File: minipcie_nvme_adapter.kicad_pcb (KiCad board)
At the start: 4 copper layers, 63.7 x 23.6 mm, 13 parts, among them J1 Bus_PCI_Express_Mini, J2 Bus_M.2_Socket_M

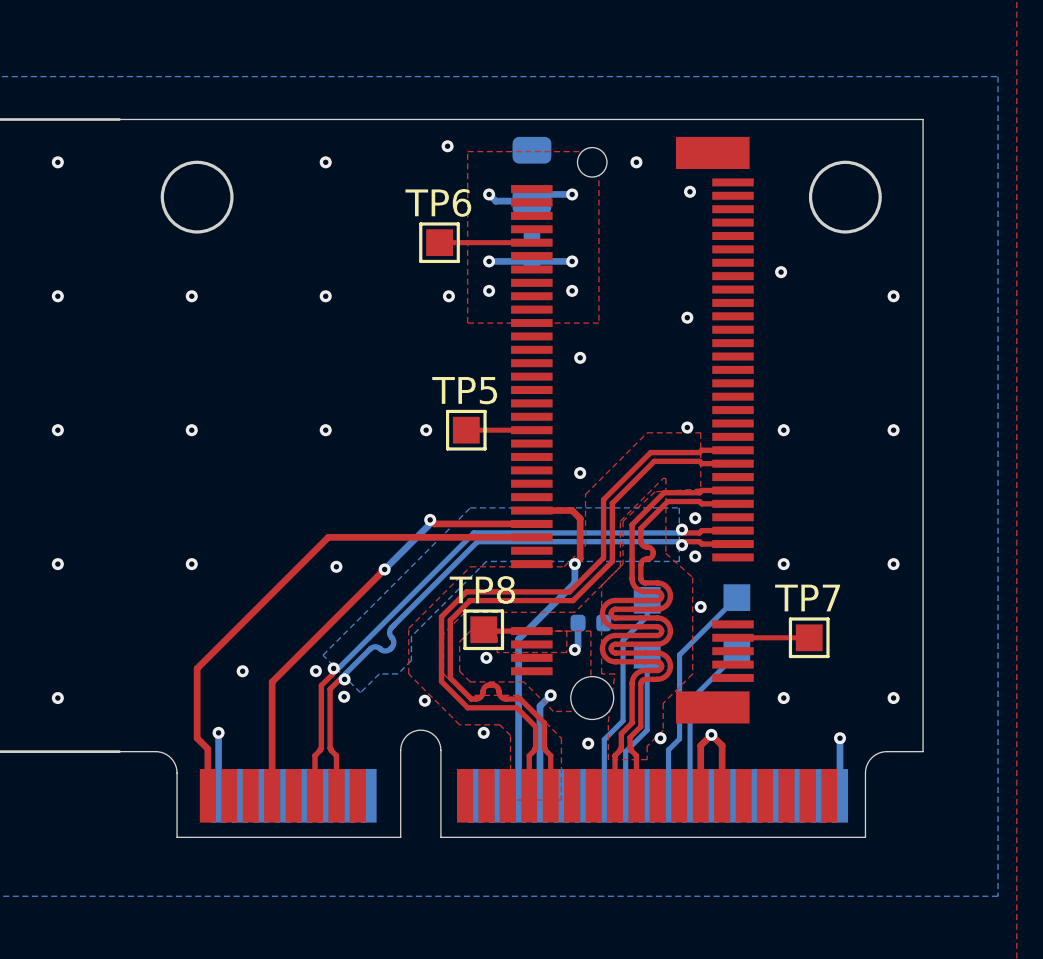
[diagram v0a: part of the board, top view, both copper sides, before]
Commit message: Fix minimum track width, re-route differential pairs, and shrink the size of the holes so that the head of my M1.6 screws don't fit through the gap.
Also inline the mpcie-half-card.kicad_mod file into this project instead of using submodules.
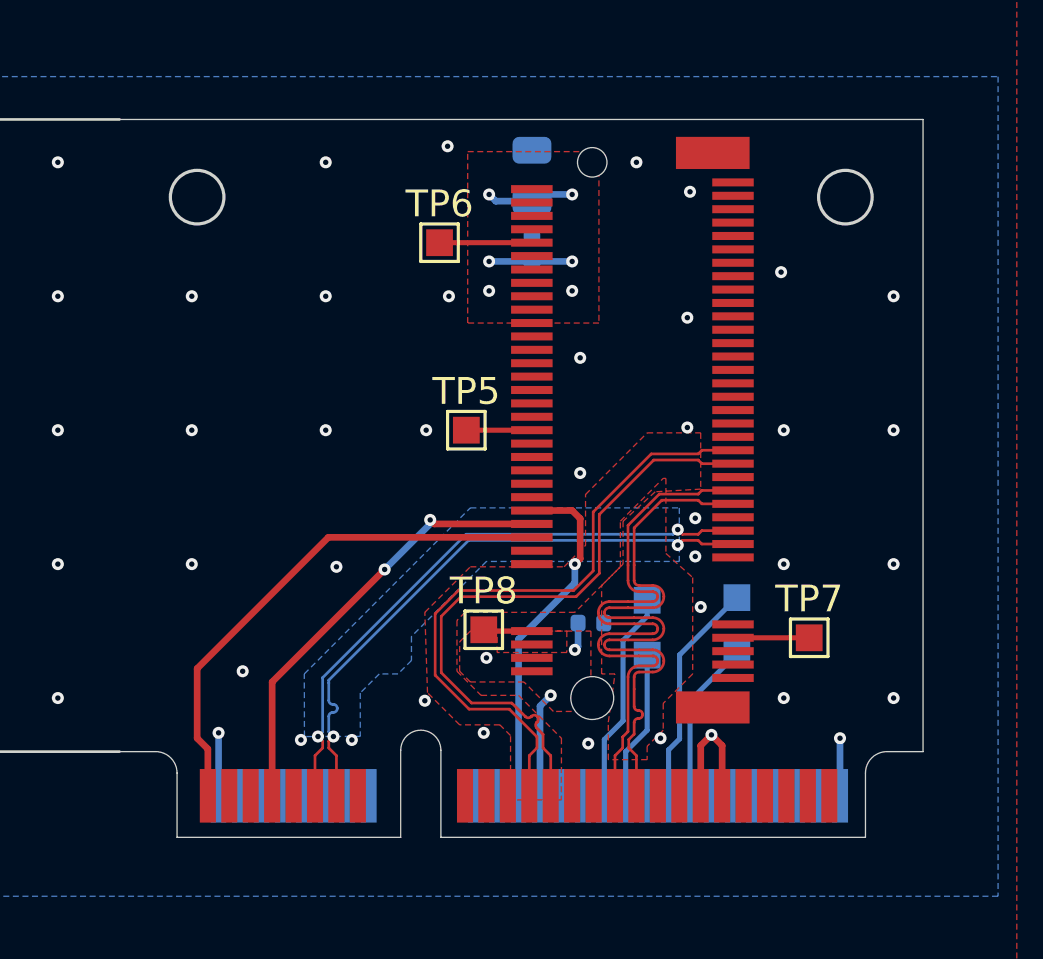
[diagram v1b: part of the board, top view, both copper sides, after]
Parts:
- J1: footprint mpcie:mpcie-half-card -> footprints:mpcie-half-card

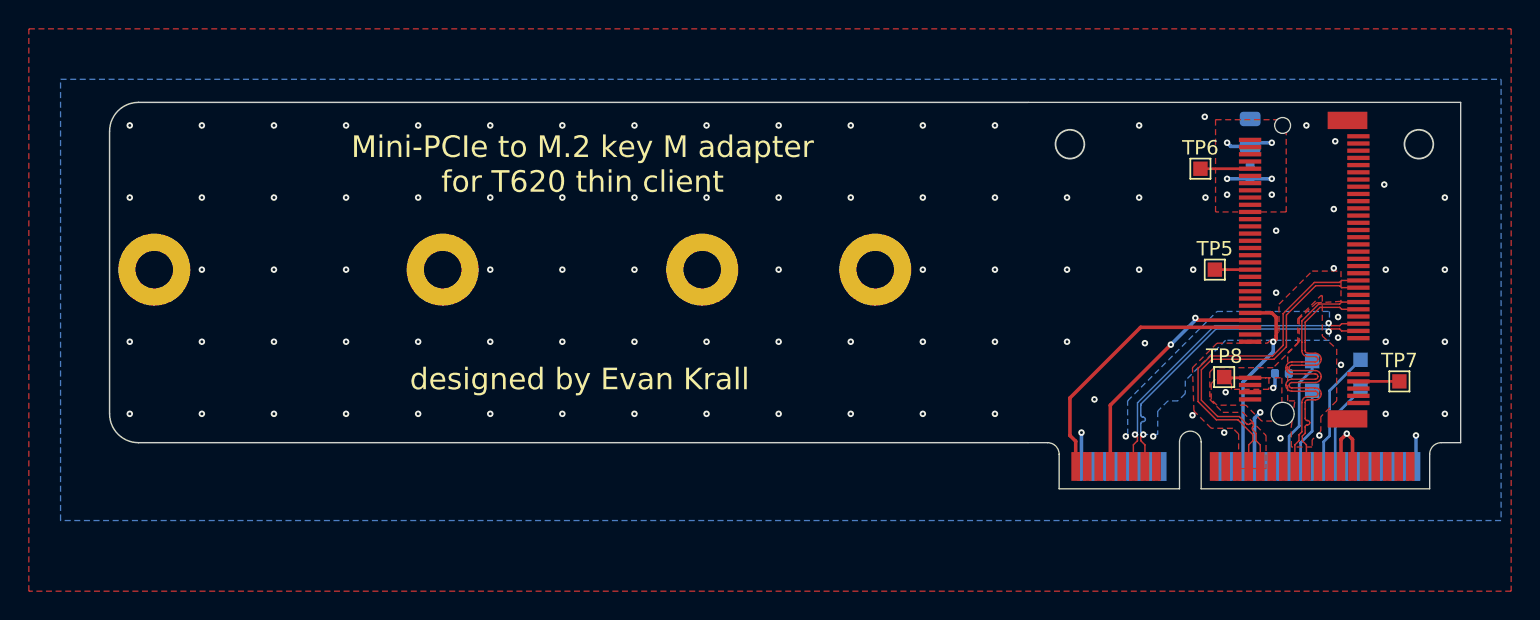
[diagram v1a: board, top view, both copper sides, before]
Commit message: Add a little cutout to avoid physical conflict with the existing 2242 SSD.
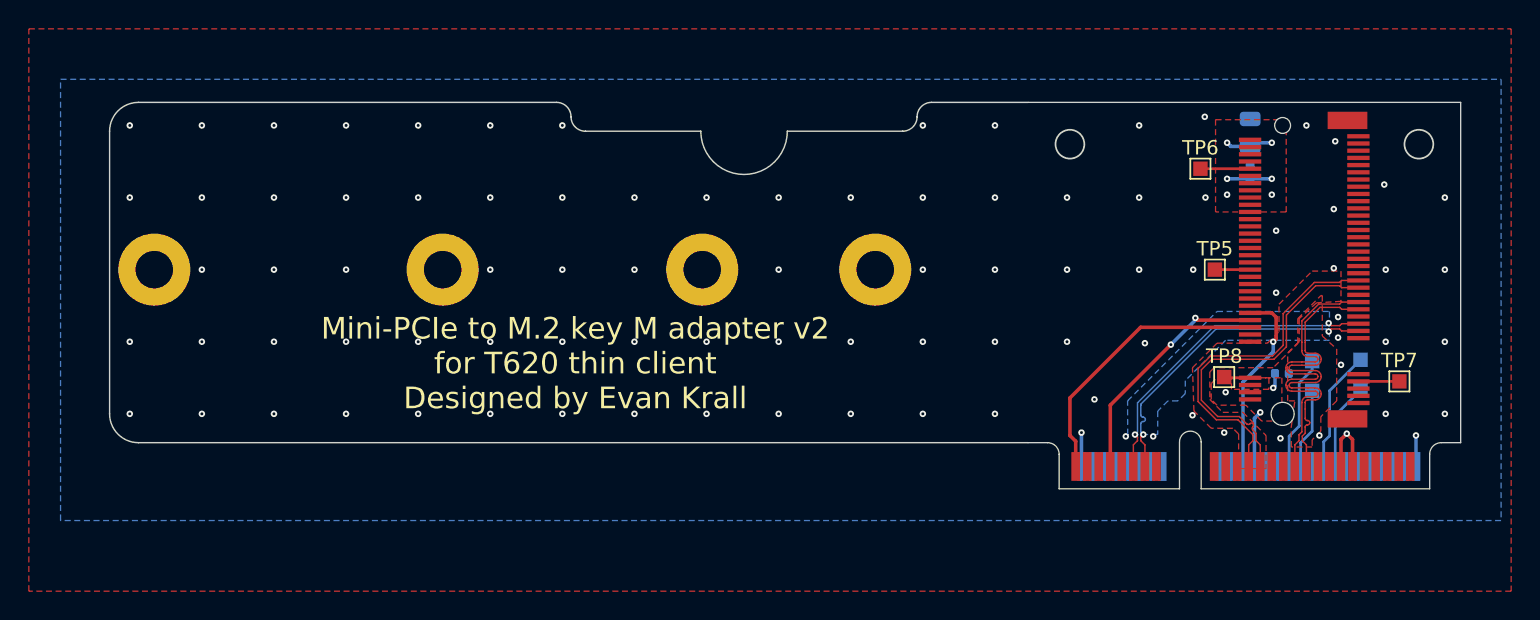
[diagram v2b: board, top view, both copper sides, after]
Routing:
- net GND: vias 95 -> 91
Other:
- outline, holes or cut-outs redrawn
- board text added: "Mini-PCIe to M.2 key M adapter v2 for T620 thin client Designed by Evan Krall"
- board text removed: "Mini-PCIe to M.2 key M adapter for T620 thin client"
- board text removed: "designed by Evan Krall"
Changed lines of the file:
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@@
   (gr_arc (start 96 91.1) (mid 94.585786 90.514214) (end 94 89.1) (layer "Edge.Cuts") (width 0.1))
   (gr_line (start 94 69.5) (end 94 89.1) (layer "Edge.Cuts") (width 0.1))
-  (gr_line (start 157.7 67.5) (end 96 67.5) (layer "Edge.Cuts") (width 0.1))
+  (gr_line (start 149 69.5) (end 141 69.5) (layer "Edge.Cuts") (width 0.1))
+  (gr_line (start 135 69.5) (end 127 69.5) (layer "Edge.Cuts") (width 0.1))
+  (gr_line (start 125 67.5) (end 96 67.5) (layer "Edge.Cuts") (width 0.1))
+  (gr_line (start 157.7 67.5) (end 151 67.5) (layer "Edge.Cuts") (width 0.1))
   (gr_line (start 157.7 91.1) (end 96 91.1) (layer "Edge.Cuts") (width 0.1))
+  (gr_arc (start 125 67.5) (mid 125.707107 67.792893) (end 126 68.5) (layer "Edge.Cuts") (width 0.1))
+  (gr_arc (start 127 69.5) (mid 126.292893 69.207107) (end 126 68.5) (layer "Edge.Cuts") (width 0.1))
+  (gr_arc (start 141 69.5) (mid 138 72.5) (end 135 69.5) (layer "Edge.Cuts") (width 0.1))
+  (gr_arc (start 150 68.5) (mid 149.707107 69.207107) (end 149 69.5) (layer "Edge.Cuts") (width 0.1))
   (gr_arc (start 94 69.5) (mid 94.585786 68.085786) (end 96 67.5) (layer "Edge.Cuts") (width 0.1))
+  (gr_arc (start 150 68.5) (mid 150.292893 67.792893) (end 151 67.5) (layer "Edge.Cuts") (width 0.1))
   (gr_text "JLCJLCJLCJLC" (at 126.8 87.1) (layer "B.SilkS")
     (effects (font (size 1 1) (thickness 0.15)) (justify mirror))
   )
-  (gr_text "designed by Evan Krall" (at 126.6 86.7) (layer "F.SilkS")
-    (effects (font (size 1.5 1.5) (thickness 0.15)))
-  )
-  (gr_text "Mini-PCIe to M.2 key M adapter\nfor T620 thin client" (at 126.8 71.8) (layer "F.SilkS")
+  (gr_text "Mini-PCIe to M.2 key M adapter v2\nfor T620 thin client\nDesigned by Evan Krall" (at 126.3 85.6) (layer "F.SilkS")
     (effects (font (size 1.5 1.5) (thickness 0.15)))
   )
@@
   (via (at 145.4 84.1) (size 0.45) (drill 0.2) (layers "F.Cu" "B.Cu") (free) (net 4))
   (via (at 100.4 79.1) (size 0.45) (drill 0.2) (layers "F.Cu" "B.Cu") (free) (net 4))
-  (via (at 130.4 69.1) (size 0.45) (drill 0.2) (layers "F.Cu" "B.Cu") (free) (net 4))
-  (via (at 145.4 69.1) (size 0.45) (drill 0.2) (layers "F.Cu" "B.Cu") (free) (net 4))
   (via (at 179.196753 83.813368) (size 0.45) (drill 0.2) (layers "F.Cu" "B.Cu") (free) (net 4))
   (via (at 169.15 79.1) (size 0.45) (drill 0.2) (layers "F.Cu" "B.Cu") (free) (net 4))
@@
   (via (at 179.196753 82.386632) (size 0.45) (drill 0.2) (layers "F.Cu" "B.Cu") (free) (net 4))
   (via (at 171.3 90.4) (size 0.45) (drill 0.2) (layers "F.Cu" "B.Cu") (free) (net 4))
-  (via (at 140.4 69.1) (size 0.45) (drill 0.2) (layers "F.Cu" "B.Cu") (free) (net 4))
   (via (at 140.4 84.1) (size 0.45) (drill 0.2) (layers "F.Cu" "B.Cu") (free) (net 4))
   (via (at 182.5 84.1) (size 0.45) (drill 0.2) (layers "F.Cu" "B.Cu") (free) (net 4))
@@
   (via (at 150.4 84.1) (size 0.45) (drill 0.2) (layers "F.Cu" "B.Cu") (free) (net 4))
   (via (at 177.9 90.6) (size 0.45) (drill 0.2) (layers "F.Cu" "B.Cu") (free) (net 4))
-  (via (at 135.4 69.1) (size 0.45) (drill 0.2) (layers "F.Cu" "B.Cu") (free) (net 4))
   (via (at 100.4 69.1) (size 0.45) (drill 0.2) (layers "F.Cu" "B.Cu") (free) (net 4))
   (via (at 179.4 85.7) (size 0.45) (drill 0.2) (layers "F.Cu" "B.Cu") (free) (net 4))
